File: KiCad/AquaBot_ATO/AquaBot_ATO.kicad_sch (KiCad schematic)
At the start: 12 parts, among them M1 Motor_DC, Q1 IRLZ44N, Q2 IRLZ44N, U1 JTD2024S05

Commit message: Improved the schematics and added a comment to the code
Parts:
- removed D2: LED_RGBK, symbol Device:LED_RGBK
- added Brd1: SSD1306, symbol SSD1306-128x64_OLED:SSD1306
- added D3: WS2812B, LED_SMD:LED_WS2812B_PLCC4_5.0x5.0mm_P3.2mm, symbol LED:WS2812B
- added J1: Conn_01x06_Socket, symbol Connector:Conn_01x06_Socket
- added J2: Conn_01x02_Socket, symbol Connector:Conn_01x02_Socket
- added J3: Conn_01x02_Pin, symbol Connector:Conn_01x02_Pin
- added J5: Conn_01x06_Pin, symbol Connector:Conn_01x06_Pin
- added R4: 470, symbol Device:R_Small
- added SW1: Push Button, symbol Switch:SW_Push
- A1: value Arduino_Nano_v3.x -> Arduino_Nano
- U1: value JTD2024S05 -> StepDown 12->5 VDC
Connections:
- net GND: now also A1.4 (GND), R1.2, U1.5 (-VOUT), Brd1.1 (GND), D3.3 (VSS), J1.2 (Pin_2), J1.5 (Pin_5), J5.2 (Pin_2), SW1.2
- net at C1.1, D1.1 (K), F1.1: now also J2.2 (Pin_2); no longer M1.1 (+)
- net at C1.2, D1.2 (A), Q1.2 (D): now also J2.1 (Pin_1); no longer M1.2 (-)
- net +5V: now reaches A1.30 (VIN), U1.3 (+VOUT)
- net +5V: now also Brd1.2 (VCC), D3.1 (VDD), J1.1 (Pin_1), J5.1 (Pin_1)
- net at A1.29 (GND): no longer U1.5 (-VOUT)
- net at Q1.1 (G), R3.1: now also J1.6 (Pin_6)
- net at A1.20 (A1), R1.1: now also J1.3 (Pin_3)
- net at A1.23 (A4): now also Brd1.4 (SDA)
- net at A1.24 (A5): now also Brd1.3 (SCL)
- net at A1.6 (D3): now also SW1.1
- net at A1.7 (D4): now also R4.2
- net +24V renamed +12V
- new net: D3.4 (DIN), J5.3 (Pin_3)
- new net: J3.2 (Pin_2), M1.1 (+)
- new net: J3.1 (Pin_1), M1.2 (-)
- new net: J1.4 (Pin_4), R4.1
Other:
- note added: "Control unit"
- note added: "High Level"
- note added: "Low Level"
- note added: "Sensor"
- note added: "Water pump"
- note removed: "High Level Pins"
- note removed: "Low Level Pins"
- moved on the sheet: C1, D1, F1, Q1, Q2, R1, R2, R3

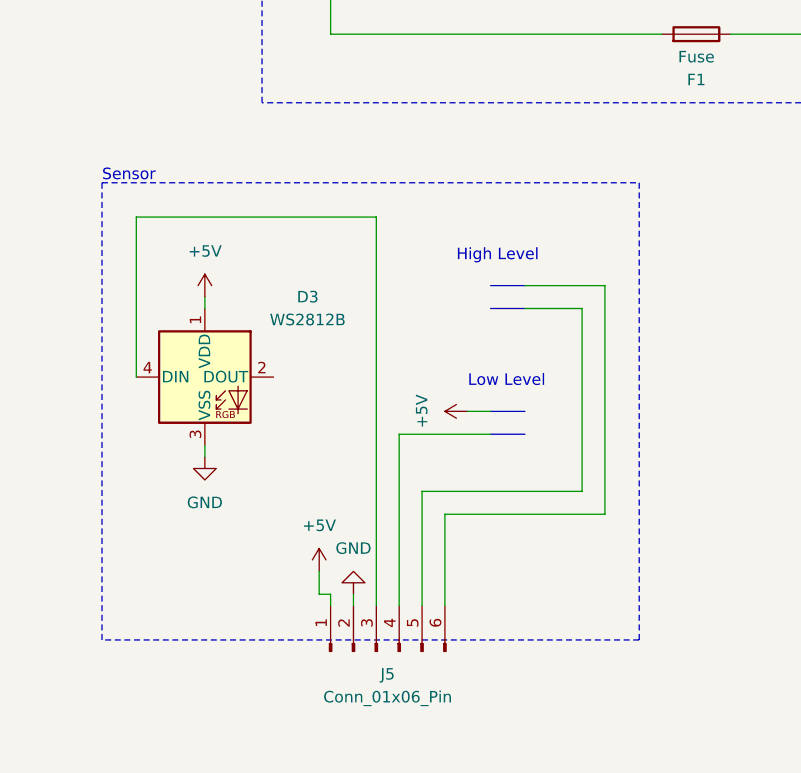
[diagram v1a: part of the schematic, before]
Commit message: Integrating a Arduino Simulation
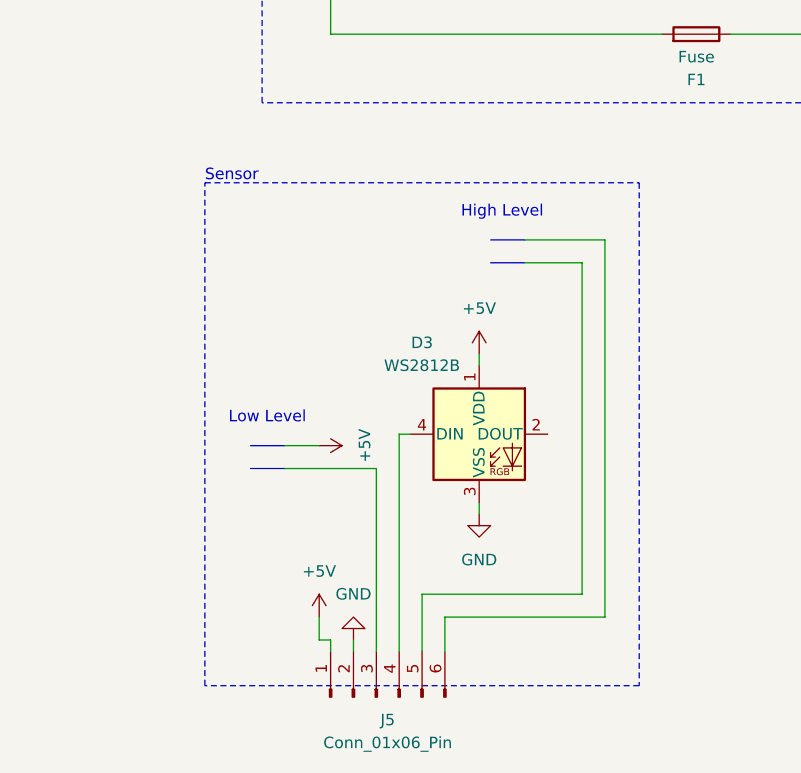
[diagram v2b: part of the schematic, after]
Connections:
- net at D3.4 (DIN): now also J5.4 (Pin_4); no longer J5.3 (Pin_3)
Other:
- moved on the sheet: D3, J5
